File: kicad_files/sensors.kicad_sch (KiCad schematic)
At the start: 42 parts, among them J1 Conn_01x01_Socket, J2 U.FL, U2 MS5611-01BA, U3 BMI088, U4 MMC5983MA, U5 MAX-M10S, U6 BMP388, U7 LSM6DSM

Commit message: reset symbol annotations
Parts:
- renumbered C26 to C20, C27 to C21, C28 to C22, C29 to C23, C30 to C24, C31 to C25, C32 to C26, C33 to C27, C34 to C28, C35 to C29, C36 to C30, C37 to C31, C38 to C32, C39 to C33, C40 to C34, C41 to C35, C42 to C36, C43 to C37, C44 to C38, C45 to C39, C46 to C40, C47 to C41, C48 to C42, R3 to R2, R4 to R3, R5 to R4, R6 to R5, R7 to R6, R8 to R7, R9 to R8, R10 to R9

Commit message: add footprint
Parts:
- C37: value 10μf -> 1μf; footprint Capacitor_SMD:C_0805_2012Metric -> Capacitor_SMD:C_0402_1005Metric
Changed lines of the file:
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@@
 			)
 		)
-		(property "Value" "10μf"
+		(property "Value" "1μf"
 			(at 184.15 36.8235 0)
 			(show_name no)
@@
 			)
 		)
-		(property "Footprint" "Capacitor_SMD:C_0805_2012Metric"
+		(property "Footprint" "Capacitor_SMD:C_0402_1005Metric"
 			(at 181.61 35.56 0)
 			(hide yes)

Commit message: Use more robust terminal block
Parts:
- J1: footprint (none) -> Connector_PinHeader_1.27mm:PinHeader_1x01_P1.27mm_Horizontal
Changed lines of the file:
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@@
 			)
 		)
-		(property "Footprint" ""
+		(property "Footprint" "Connector_PinHeader_1.27mm:PinHeader_1x01_P1.27mm_Horizontal"
 			(at 119.38 116.84 0)
 			(hide yes)

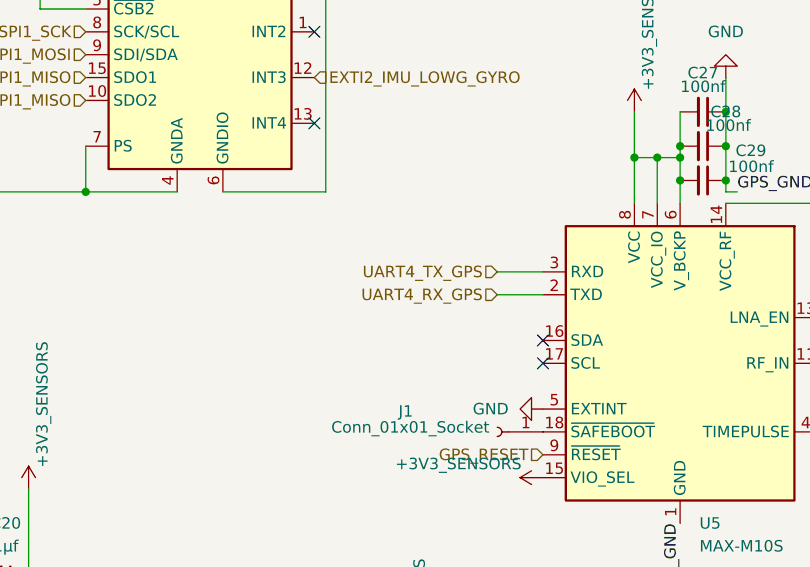
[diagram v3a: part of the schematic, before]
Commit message: switch uart, usart, spi lines, adc, pwm
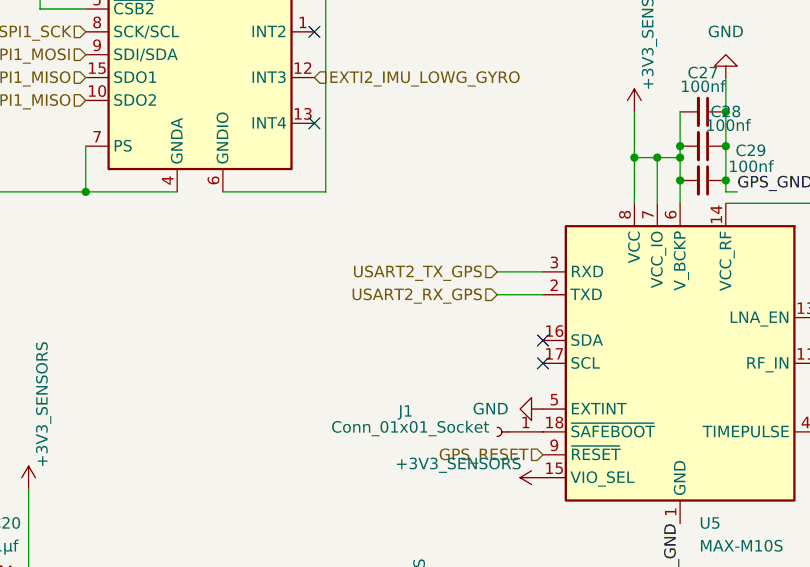
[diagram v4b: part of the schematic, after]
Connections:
- net UART4_RX_GPS renamed USART2_RX_GPS
- net UART4_TX_GPS renamed USART2_TX_GPS
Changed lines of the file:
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@@
 		)
 	)
-	(hierarchical_label "UART4_RX_GPS"
+	(hierarchical_label "USART2_RX_GPS"
 		(shape input)
 		(at 119.38 101.6 180)
@@
 		)
 	)
-	(hierarchical_label "UART4_TX_GPS"
+	(hierarchical_label "USART2_TX_GPS"
 		(shape input)
 		(at 119.38 99.06 180)

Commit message: impedance match u.fl line
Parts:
- J2: footprint PCM_JLCPCB:IPEX-SMD_BWIPX-1-001E -> Connector_Coaxial:U.FL_Hirose_U.FL-R-SMT-1_Vertical
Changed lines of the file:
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@@
 			)
 		)
-		(property "Footprint" "PCM_JLCPCB:IPEX-SMD_BWIPX-1-001E"
+		(property "Footprint" "Connector_Coaxial:U.FL_Hirose_U.FL-R-SMT-1_Vertical"
 			(at 180.34 109.22 0)
 			(hide yes)

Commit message: fix unconnected
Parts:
- removed C24: 1μf, Capacitor_SMD:C_0402_1005Metric, symbol Device:C_Small
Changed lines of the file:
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@@
 	)
 	(junction
-		(at 88.9 48.26)
-		(diameter 0)
-		(color 0 0 0 0)
-	)
-	(junction
 		(at 248.92 43.18)
 		(diameter 0)
@@
 	)
 	(junction
-		(at 93.98 48.26)
-		(diameter 0)
-		(color 0 0 0 0)
-	)
-	(junction
 		(at 175.26 91.44)
 		(diameter 0)
@@
 	(wire
 		(pts
-			(xy 93.98 45.72) (xy 93.98 48.26)
+			(xy 93.98 45.72) (xy 93.98 57.15)
 		)
 		(stroke
@@
 	(wire
 		(pts
-			(xy 88.9 38.1) (xy 88.9 48.26)
+			(xy 88.9 38.1) (xy 88.9 57.15)
 		)
 		(stroke
@@
 	(wire
 		(pts
-			(xy 88.9 48.26) (xy 88.9 57.15)
-		)
-		(stroke
-			(width 0)
-			(type default)
-		)
-	)
-	(wire
-		(pts
 			(xy 181.61 43.18) (xy 181.61 55.88)
 		)
@@
 	(wire
 		(pts
-			(xy 93.98 48.26) (xy 93.98 57.15)
-		)
-		(stroke
-			(width 0)
-			(type default)
-		)
-	)
-	(wire
-		(pts
 			(xy 245.11 52.07) (xy 245.11 57.15)
 		)
@@
 					(unit 1)
 				)
-			)
-		)
-	)
-	(symbol
-		(lib_id "Device:C_Small")
-		(at 91.44 48.26 270)
-		(unit 1)
-		(body_style 1)
-		(exclude_from_sim no)
-		(in_bom yes)
-		(on_board yes)
-		(in_pos_files yes)
-		(dnp no)
-		(fields_autoplaced yes)
-		(property "Reference" "C24"
-			(at 91.4336 41.91 90)
-			(show_name no)
-			(do_not_autoplace no)
-			(effects
-				(font
-					(size 1.27 1.27)
-				)
-			)
-		)
-		(property "Value" "1μf"
-			(at 91.4336 44.45 90)
-			(show_name no)
-			(do_not_autoplace no)
-			(effects
-				(font
-					(size 1.27 1.27)
-				)
-			)
-		)
-		(property "Footprint" "Capacitor_SMD:C_0402_1005Metric"
-			(at 91.44 48.26 0)
-			(hide yes)
-			(show_name no)
-			(do_not_autoplace no)
-			(effects
-				(font
-					(size 1.27 1.27)
-				)
-			)
-		)
-		(property "Datasheet" ""
-			(at 91.44 48.26 0)
-			(hide yes)
-			(show_name no)
-			(do_not_autoplace no)
-			(effects
-				(font
-					(size 1.27 1.27)
-				)
-			)
-		)
-		(property "Description" "Unpolarized capacitor, small symbol"
-			(at 91.44 48.26 0)
-			(hide yes)
-			(show_name no)
-			(do_not_autoplace no)
-			(effects
-				(font
-					(size 1.27 1.27)
-				)
-			)
-		)
-		(pin "2"
-		)
-		(pin "1"
-		)
-		(instances
-			(project "versorlite"
-				(path "/1a230af0-0a74-48f7-8607-b087121dda49/11200af7-3897-4179-b08c-df8c2996a93a"
-					(reference "C24")
-					(unit 1)
-				)

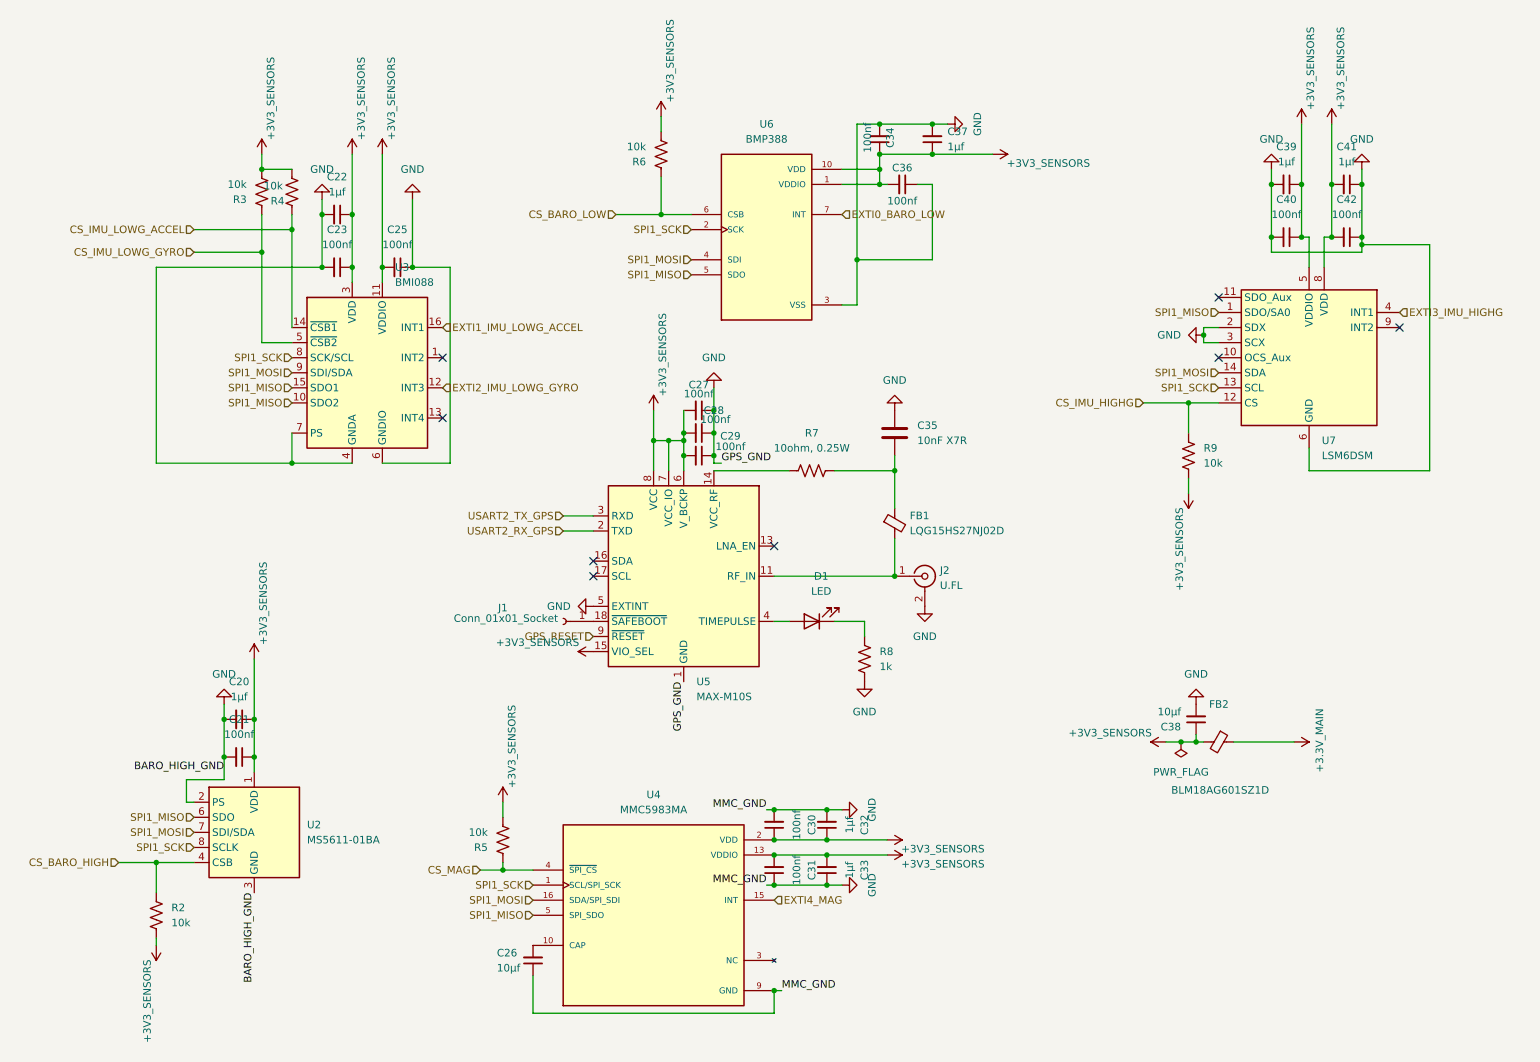
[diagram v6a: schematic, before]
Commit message: add dedicated power switching
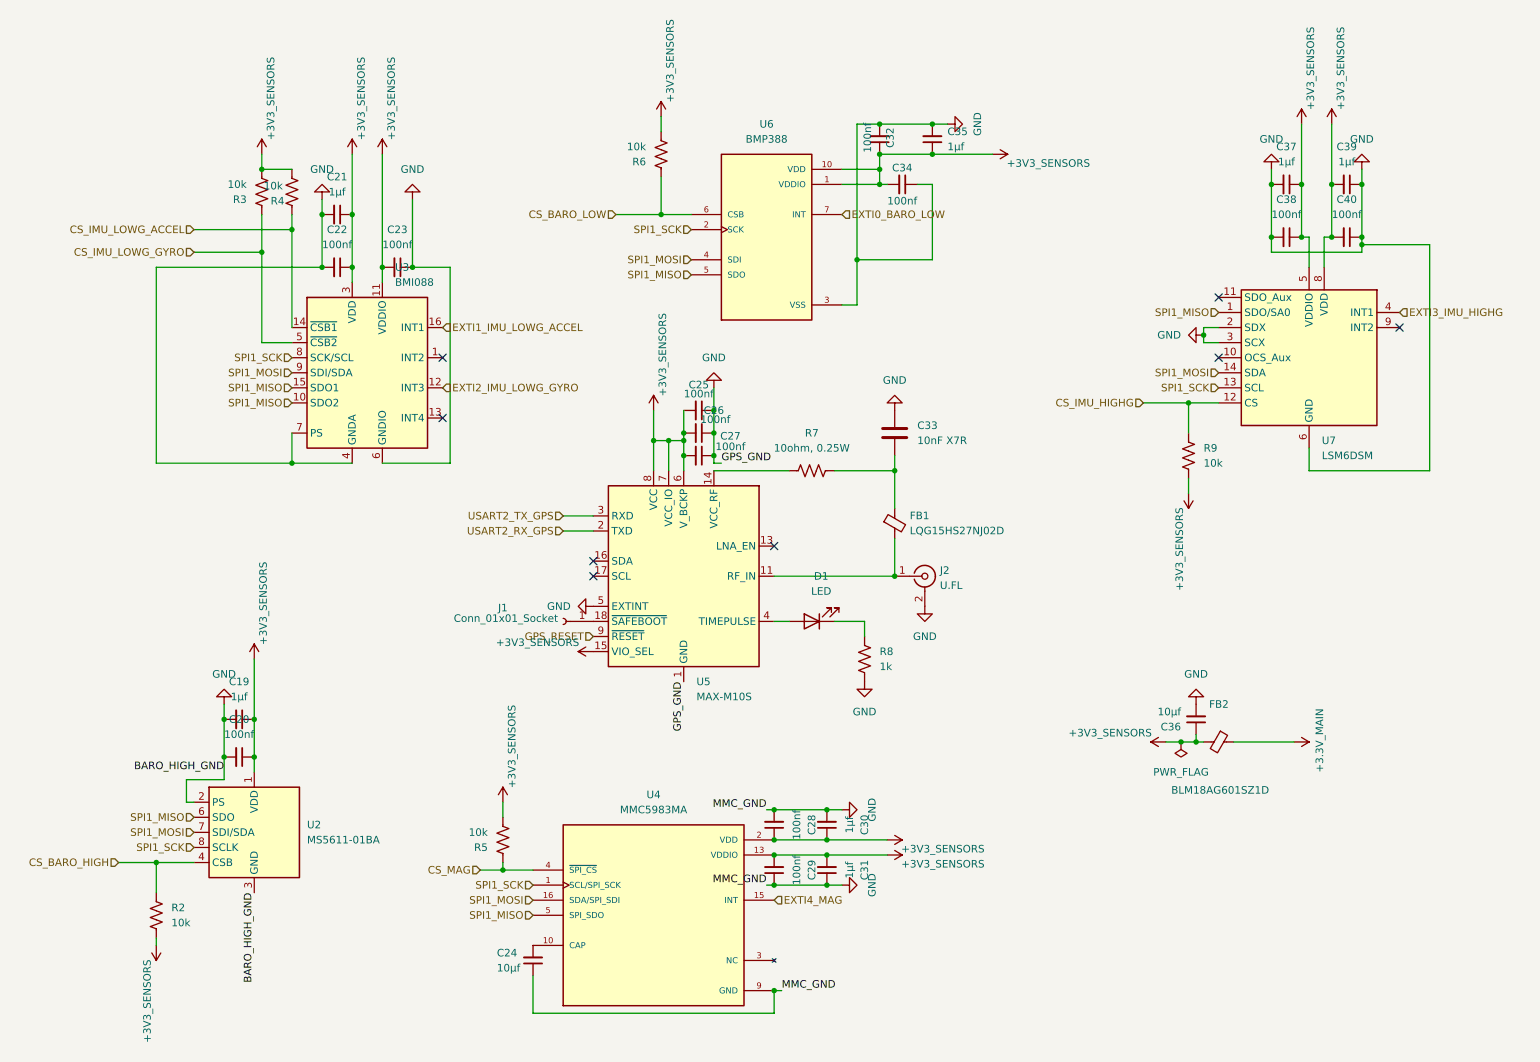
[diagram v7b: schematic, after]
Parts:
- renumbered C20 to C19, C21 to C20, C22 to C21, C23 to C22, C25 to C23, C26 to C24, C27 to C25, C28 to C26, C29 to C27, C30 to C28, C31 to C29, C32 to C30, C33 to C31, C34 to C32, C35 to C33, C36 to C34, C37 to C35, C38 to C36, C39 to C37, C40 to C38, C41 to C39, C42 to C40

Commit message: add pwm tht hole
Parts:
- J1: footprint Connector_PinHeader_1.27mm:PinHeader_1x01_P1.27mm_Horizontal -> TestPoint:TestPoint_Pad_D1.0mm
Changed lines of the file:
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@@
 			)
 		)
-		(property "Footprint" "Connector_PinHeader_1.27mm:PinHeader_1x01_P1.27mm_Horizontal"
+		(property "Footprint" "TestPoint:TestPoint_Pad_D1.0mm"
 			(at 119.38 116.84 0)
 			(hide yes)
